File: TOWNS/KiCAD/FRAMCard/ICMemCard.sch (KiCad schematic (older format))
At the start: 17 parts, among them J1 PCMCIA_Connector, Q1 BC846X, Q2 BC846X, U1 FM18W08-SGTR, U2 FM18W08-SGTR, U3 74AHCT1G32

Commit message: Working on PCB for NX1 PCMCIA frame.
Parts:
- U3: footprint (none) -> PCMCIA:SOT353_Easy
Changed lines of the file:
@@
 F 0 "U3" H 4725 6067 50  0000 C CNN
 F 1 "74AHCT1G32" H 4725 5976 50  0000 C CNN
-F 2 "" H 4750 5800 50  0001 C CNN
+F 2 "PCMCIA:SOT353_Easy" H 4750 5800 50  0001 C CNN
 F 3 "http://www.ti.com/lit/sg/scyt129e/scyt129e.pdf" H 4750 5800 50  0001 C CNN
 	1    4750 5800

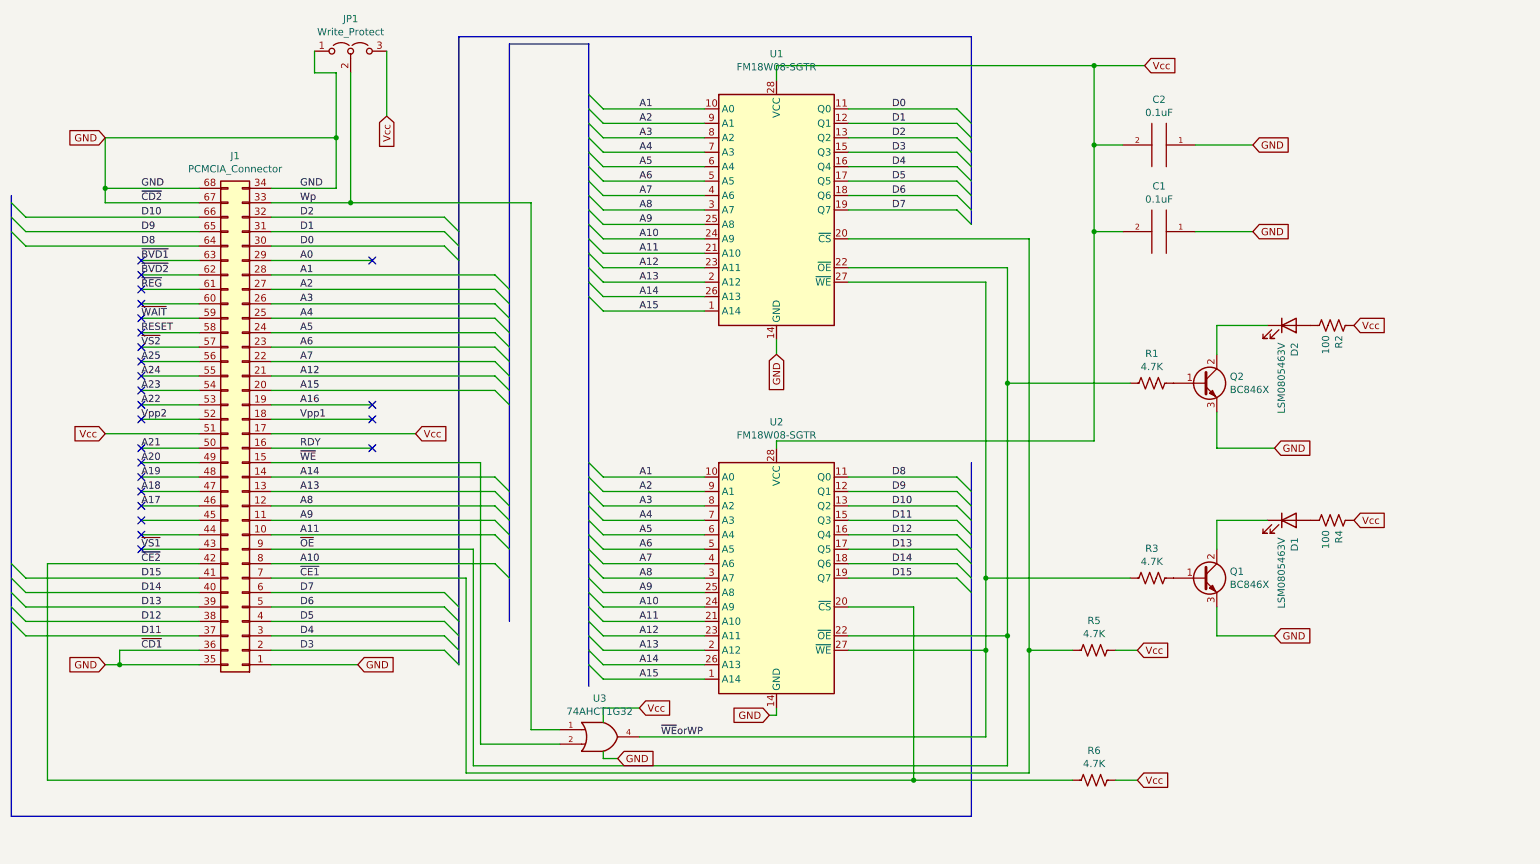
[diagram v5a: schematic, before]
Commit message: Use 74LS32 instead of 1-CH OR gate.  Easier soldering.
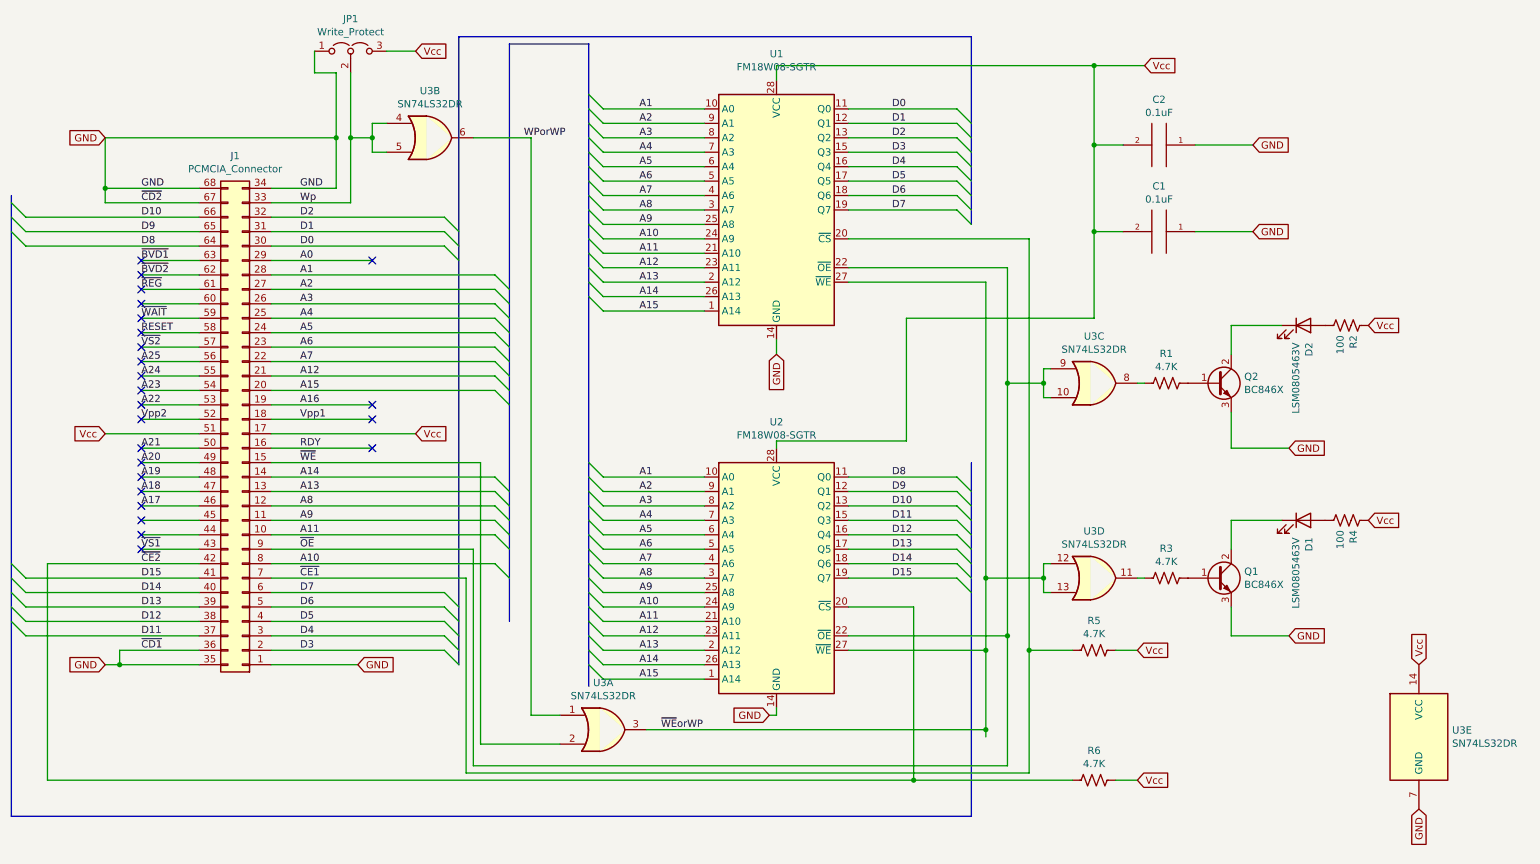
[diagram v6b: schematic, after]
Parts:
- removed U3: 74AHCT1G32, PCMCIA:SOT353_Easy, symbol 74xGxx:74AHCT1G32
- added U3: SN74LS32DR, Package_SO:SOIC-14_3.9x8.7mm_P1.27mm, symbol 74xx:74LS32
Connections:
- net GND: now also U3.7 (GND)
- net Wp: now also U3.4, U3.5
- net ~OE: now also U3.10, U3.9; no longer R1.2
- net ~WE: now also U3.2
- net ~WE~orWP: now also U3.12, U3.13, U3.3; no longer R3.2
- net VCC renamed Vcc
- net Vcc: now also U3.14 (VCC)
- new net: R3.2, U3.11
- new net: R1.2, U3.8
- new net WPorWP: U3.1, U3.6
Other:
- moved on the sheet: D1, D2, Q1, Q2, R1, R2, R3, R4

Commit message: Cleaning up vias.
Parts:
- R1, R2, R3, R4, R5, R6: footprint PCMCIA:KOA_RK73G2AAT -> Resistor_SMD:R_0805_2012Metric_Pad1.15x1.40mm_HandSolder
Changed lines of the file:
@@
 F 0 "R3" V 8445 4700 50  0000 C CNN
 F 1 "4.7K" V 8536 4700 50  0000 C CNN
-F 2 "PCMCIA:KOA_RK73G2AAT" V 8690 4690 50  0001 C CNN
+F 2 "Resistor_SMD:R_0805_2012Metric_Pad1.15x1.40mm_HandSolder" V 8690 4690 50  0001 C CNN
 F 3 "~" H 8650 4700 50  0001 C CNN
 	1    8650 4700
@@
 F 0 "R4" H 9968 4346 50  0000 L CNN
 F 1 "100" H 9968 4255 50  0000 L CNN
-F 2 "PCMCIA:KOA_RK73G2AAT" V 9940 4290 50  0001 C CNN
+F 2 "Resistor_SMD:R_0805_2012Metric_Pad1.15x1.40mm_HandSolder" V 9940 4290 50  0001 C CNN
 F 3 "~" H 9900 4300 50  0001 C CNN
 	1    9900 4300
@@
 F 0 "R1" V 8445 3350 50  0000 C CNN
 F 1 "4.7K" V 8536 3350 50  0000 C CNN
-F 2 "PCMCIA:KOA_RK73G2AAT" V 8690 3340 50  0001 C CNN
+F 2 "Resistor_SMD:R_0805_2012Metric_Pad1.15x1.40mm_HandSolder" V 8690 3340 50  0001 C CNN
 F 3 "~" H 8650 3350 50  0001 C CNN
 	1    8650 3350
@@
 F 0 "R2" H 9968 2996 50  0000 L CNN
 F 1 "100" H 9968 2905 50  0000 L CNN
-F 2 "PCMCIA:KOA_RK73G2AAT" V 9940 2940 50  0001 C CNN
+F 2 "Resistor_SMD:R_0805_2012Metric_Pad1.15x1.40mm_HandSolder" V 9940 2940 50  0001 C CNN
 F 3 "~" H 9900 2950 50  0001 C CNN
 	1    9900 2950
@@
 F 0 "R5" V 7945 5200 50  0000 C CNN
 F 1 "4.7K" V 8036 5200 50  0000 C CNN
-F 2 "PCMCIA:KOA_RK73G2AAT" V 8190 5190 50  0001 C CNN
+F 2 "Resistor_SMD:R_0805_2012Metric_Pad1.15x1.40mm_HandSolder" V 8190 5190 50  0001 C CNN
 F 3 "~" H 8150 5200 50  0001 C CNN
 	1    8150 5200
@@
 F 0 "R6" V 7945 6100 50  0000 C CNN
 F 1 "4.7K" V 8036 6100 50  0000 C CNN
-F 2 "PCMCIA:KOA_RK73G2AAT" V 8190 6090 50  0001 C CNN
+F 2 "Resistor_SMD:R_0805_2012Metric_Pad1.15x1.40mm_HandSolder" V 8190 6090 50  0001 C CNN
 F 3 "~" H 8150 6100 50  0001 C CNN
 	1    8150 6100
@@
 Wire Wire Line
 	6850 2900 6850 3750
-Wire Bus Line
-	3750 950  3750 5300
-Wire Bus Line
-	7300 950  7300 2250
-Wire Bus Line
-	650  2050 650  6350
-Wire Bus Line
-	7300 3900 7300 6350
-Wire Bus Line
-	4100 1000 4100 5000
-Wire Bus Line
-	4650 1000 4650 5450
 Wire Wire Line
 	6850 3750 5950 3750
 Text Label 4200 1650 0    50   ~ 0
 WPorWP
+Wire Bus Line
+	3750 950  3750 5300
+Wire Bus Line
+	7300 950  7300 2250
+Wire Bus Line
+	650  2050 650  6350
+Wire Bus Line
+	7300 3900 7300 6350
+Wire Bus Line
+	4100 1000 4100 5000
+Wire Bus Line
+	4650 1000 4650 5450
 $EndSCHEMATC

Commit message: Updated Schematic and PCB.
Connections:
- net GND: now also U3.4, U3.5
- net ~OE: now also R1.2; no longer U3.10, U3.9
- net ~WE~orWP: now also R3.2; no longer U3.12, U3.13
- net at U3.11: no longer R3.2
- net at U3.8: now also U3.12, U3.13; no longer R1.2
- net WPorWP: no longer names the net of U3.6
- net WPorWP: now also U3.10, U3.9; no longer U3.1
- net Wp renamed WP
- net WP: now also U3.1; no longer U3.4, U3.5
- no-connect marks 24 -> 25
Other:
- moved on the sheet: U3B, U3C, U3D
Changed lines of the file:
@@
 Wire Wire Line
 	1950 4800 750  4800
-Wire Wire Line
-	1950 5300 1400 5300
 $Comp
 L Connector_Generic:Conn_02x34_Top_Bottom J1
@@
 	7400 5750 7400 5200
 Wire Wire Line
-	3150 1750 3250 1750
-Wire Wire Line
-	3250 1550 3150 1550
+	4250 1650 4250 5650
+$Comp
+L 74xx:74LS32 U3
+U 4 1 6289CCA8
+P 3300 5800
+F 0 "U3" H 3300 6125 50  0000 C CNN
+F 1 "SN74LS32DR" H 3300 6034 50  0000 C CNN
+F 2 "Package_SO:SOIC-14_3.9x8.7mm_P1.27mm" H 3300 5800 50  0001 C CNN
+F 3 "http://www.ti.com/lit/gpn/sn74LS32" H 3300 5800 50  0001 C CNN
+	4    3300 5800
+	1    0    0    -1
+$EndComp
+Wire Wire Line
+	7400 4700 7400 2650
+Wire Wire Line
+	7400 5200 7400 4700
+Connection ~ 7400 4700
+$Comp
+L 74xx:74LS32 U3
+U 3 1 6289C4F4
+P 2550 5800
+F 0 "U3" H 2550 6125 50  0000 C CNN
+F 1 "SN74LS32DR" H 2550 6034 50  0000 C CNN
+F 2 "Package_SO:SOIC-14_3.9x8.7mm_P1.27mm" H 2550 5800 50  0001 C CNN
+F 3 "http://www.ti.com/lit/gpn/sn74LS32" H 2550 5800 50  0001 C CNN
+	3    2550 5800
+	1    0    0    -1
+$EndComp
+Wire Wire Line
+	7550 2550 7550 3350
+Wire Wire Line
+	7550 5100 7550 3350
+Connection ~ 7550 3350
+Wire Wire Line
+	8150 2900 6850 2900
+Wire Wire Line
+	6850 2900 6850 3750
+Wire Wire Line
+	6850 3750 5950 3750
+Text Label 4200 1650 0    50   ~ 0
+WP
+Wire Wire Line
+	3000 1200 3000 1650
+Wire Wire Line
+	3000 1650 4250 1650
+Connection ~ 3000 1650
+Wire Wire Line
+	3000 1650 3000 2100
+Wire Wire Line
+	7550 3350 8500 3350
+Wire Wire Line
+	7400 4700 8500 4700
+Wire Wire Line
+	2950 5900 3000 5900
+Wire Wire Line
+	3000 5700 2950 5700
+Wire Wire Line
+	2950 5700 2950 5800
+Wire Wire Line
+	2250 5900 2150 5900
+Wire Wire Line
+	2150 5900 2150 5800
+Wire Wire Line
+	2250 5700 2150 5700
+NoConn ~ 3600 5800
+Wire Wire Line
+	1400 5300 1950 5300
 $Comp
 L 74xx:74LS32 U3
 U 2 1 6289995C
-P 3550 1650
-F 0 "U3" H 3550 1975 50  0000 C CNN
-F 1 "SN74LS32DR" H 3550 1884 50  0000 C CNN
-F 2 "Package_SO:SOIC-14_3.9x8.7mm_P1.27mm" H 3550 1650 50  0001 C CNN
-F 3 "http://www.ti.com/lit/gpn/sn74LS32" H 3550 1650 50  0001 C CNN
-	2    3550 1650
-	1    0    0    -1
-$EndComp
-Wire Wire Line
-	3150 1550 3150 1650
-Wire Wire Line
-	3000 1200 3000 1650
-Wire Wire Line
-	3000 1650 3150 1650
-Connection ~ 3000 1650
-Wire Wire Line
-	3000 1650 3000 2100
-Connection ~ 3150 1650
-Wire Wire Line
-	3150 1650 3150 1750
-Wire Wire Line
-	3850 1650 4250 1650
-Wire Wire Line
-	4250 1650 4250 5650
-$Comp
-L 74xx:74LS32 U3
-U 4 1 6289CCA8
-P 8150 4700
-F 0 "U3" H 8150 5025 50  0000 C CNN
-F 1 "SN74LS32DR" H 8150 4934 50  0000 C CNN
-F 2 "Package_SO:SOIC-14_3.9x8.7mm_P1.27mm" H 8150 4700 50  0001 C CNN
-F 3 "http://www.ti.com/lit/gpn/sn74LS32" H 8150 4700 50  0001 C CNN
-	4    8150 4700
-	1    0    0    -1
-$EndComp
-Wire Wire Line
-	7400 4700 7400 2650
-Wire Wire Line
-	7400 5200 7400 4700
-Connection ~ 7400 4700
-$Comp
-L 74xx:74LS32 U3
-U 3 1 6289C4F4
-P 8150 3350
-F 0 "U3" H 8150 3675 50  0000 C CNN
-F 1 "SN74LS32DR" H 8150 3584 50  0000 C CNN
-F 2 "Package_SO:SOIC-14_3.9x8.7mm_P1.27mm" H 8150 3350 50  0001 C CNN
-F 3 "http://www.ti.com/lit/gpn/sn74LS32" H 8150 3350 50  0001 C CNN
-	3    8150 3350
-	1    0    0    -1
-$EndComp
-Wire Wire Line
-	7550 2550 7550 3350
-Wire Wire Line
-	7550 5100 7550 3350
-Connection ~ 7550 3350
-Wire Wire Line
-	7550 3350 7800 3350
-Wire Wire Line
-	7800 3350 7800 3250
-Wire Wire Line
-	7800 3250 7850 3250
-Connection ~ 7800 3350
-Wire Wire Line
-	7800 3350 7800 3450
-Wire Wire Line
-	7800 3450 7850 3450
-Wire Wire Line
-	7800 4600 7850 4600
-Wire Wire Line
-	7800 4600 7800 4700
-Connection ~ 7800 4700
-Wire Wire Line
-	7800 4700 7400 4700
-Wire Wire Line
-	7800 4700 7800 4800
-Wire Wire Line
-	7800 4800 7850 4800
-Wire Wire Line
-	8450 3350 8500 3350
-Wire Wire Line
-	8450 4700 8500 4700
-Wire Wire Line
-	8150 2900 6850 2900
-Wire Wire Line
-	6850 2900 6850 3750
-Wire Wire Line
-	6850 3750 5950 3750
-Text Label 4200 1650 0    50   ~ 0
-WPorWP
+P 1800 5800
+F 0 "U3" H 1800 6125 50  0000 C CNN
+F 1 "SN74LS32DR" H 1800 6034 50  0000 C CNN
+F 2 "Package_SO:SOIC-14_3.9x8.7mm_P1.27mm" H 1800 5800 50  0001 C CNN
+F 3 "http://www.ti.com/lit/gpn/sn74LS32" H 1800 5800 50  0001 C CNN
+	2    1800 5800
+	1    0    0    -1
+$EndComp
+Wire Wire Line
+	1400 5700 1500 5700
+Wire Wire Line
+	1400 5900 1500 5900
+Wire Wire Line
+	1400 5700 1400 5900
+Connection ~ 1400 5700
+Wire Wire Line
+	1400 5300 1400 5700
+Wire Wire Line
+	2100 5800 2150 5800
+Connection ~ 2150 5800
+Wire Wire Line
+	2150 5800 2150 5700
+Wire Wire Line
+	2850 5800 2950 5800
 Wire Bus Line
 	3750 950  3750 5300
@@
 Wire Bus Line
 	4650 1000 4650 5450
+Connection ~ 2950 5800
+Wire Wire Line
+	2950 5800 2950 5900
 $EndSCHEMATC
